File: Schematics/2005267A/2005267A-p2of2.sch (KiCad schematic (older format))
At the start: 4 parts, among them J3 ConnectorA1-300, J4 ConnectorA1-400, X2 ArrowTwiddle, X3 ArrowTwiddle

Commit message: Finished sheet 2 (and hence the complete set of sheets) of CAD drawing 2005267A.
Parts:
- removed X2, X3: ArrowTwiddle, symbol AGC_DSKY:ArrowTwiddle
- added G301: Ground-chassis, symbol AGC_DSKY:Ground-chassis
- added unit 22 of J3
- added unit 59 of J3
- added unit 57 of J3
- added unit 54 of J3
- added unit 55 of J3
- added unit 58 of J3
- added unit 50 of J3
- added unit 53 of J3
- added unit 52 of J3
- added unit 26 of J3
- added unit 41 of J3
- added unit 46 of J3
- added unit 44 of J3
- added unit 45 of J3
- added unit 71 of J3
- added unit 70 of J3
- added unit 62 of J3
- added unit 68 of J3
- added unit 69 of J3
- added unit 61 of J3
- added unit 63 of J3
- added unit 64 of J3
- added unit 65 of J3
- added unit 66 of J3
- added unit 67 of J3
- added unit 1 of J3
- added unit 19 of J3
- added unit 18 of J3
- added unit 42 of J3
- added unit 11 of J3
- added unit 10 of J3
- added unit 15 of J3
- added unit 43 of J3
- added unit 8 of J3
- added unit 9 of J3
- added unit 6 of J3
- added unit 4 of J3
- added unit 38 of J3
- added unit 56 of J3
- added unit 3 of J3
- added unit 37 of J3
- added unit 35 of J3
- added unit 34 of J3
- added unit 33 of J3
- added unit 32 of J3
- added unit 31 of J3
- added unit 30 of J3
- added unit 39 of J3
- added unit 17 of J3
- added unit 7 of J3
- added unit 5 of J3
- added unit 2 of J3
- added unit 40 of J3
- added unit 16 of J3
- added unit 13 of J3
- added unit 47 of J3
- added unit 25 of J3
- added unit 14 of J3
- added unit 27 of J3
- added unit 20 of J3
- added unit 23 of J3
- added unit 49 of J3
- added unit 29 of J3
- added unit 28 of J3
- added unit 64 of J4
- added unit 68 of J4
- added unit 61 of J4
- added unit 62 of J4
- added unit 63 of J4
- added unit 4 of J4
- added unit 28 of J4
- added unit 71 of J4
- added unit 1 of J4
- added unit 3 of J4
- added unit 2 of J4
- added unit 5 of J4
- added unit 7 of J4
- added unit 6 of J4
- added unit 9 of J4
- added unit 8 of J4
- added unit 22 of J4
- added unit 67 of J4
- added unit 65 of J4
- added unit 16 of J4
- added unit 17 of J4
- added unit 14 of J4
- added unit 15 of J4
- added unit 13 of J4
- added unit 10 of J4
- added unit 11 of J4
- added unit 18 of J4
- added unit 19 of J4
- added unit 32 of J4
- added unit 31 of J4
- added unit 30 of J4
- added unit 37 of J4
- added unit 29 of J4
- added unit 25 of J4
- added unit 66 of J4
- added unit 69 of J4
- added unit 38 of J4
- added unit 39 of J4
- added unit 35 of J4
- added unit 49 of J4
- added unit 45 of J4
- added unit 44 of J4
- added unit 47 of J4
- added unit 34 of J4
- added unit 46 of J4
- added unit 41 of J4
- added unit 40 of J4
- added unit 43 of J4
- added unit 42 of J4
- added unit 70 of J4
- added unit 54 of J4
- added unit 27 of J4
- added unit 26 of J4
- added unit 23 of J4
- added unit 55 of J4
- added unit 57 of J4
- added unit 56 of J4
- added unit 50 of J4
- added unit 53 of J4
- added unit 52 of J4
- added unit 59 of J4
- added unit 58 of J4
- added unit 20 of J4
- added unit 33 of J4
- added U201: D3NOR-+4SW-0VDCA-CB_-E_F, symbol D3NOR-+4SW-0VDCA:D3NOR-+4SW-0VDCA-CB_-E_F
- added U202, U207, U211, U213, U217, U219, U223, U225, U229, U233: D3NOR-+4SW-0VDCA-CB_-EF_, symbol D3NOR-+4SW-0VDCA:D3NOR-+4SW-0VDCA-CB_-EF_
- added U203, U215, U221, U227, U246: D3NOR-FAP-0VDCA-expander-BAC-EDF, symbol D3NOR-FAP-0VDCA-expander:D3NOR-FAP-0VDCA-expander-BAC-EDF
- added U204, U210, U216, U222, U228, U239: D3NOR-+4SW-0VDCA-BC_-EF_, symbol D3NOR-+4SW-0VDCA:D3NOR-+4SW-0VDCA-BC_-EF_
- added U205, U235, U238, U241, U244: D3NOR-+4SW-0VDCA-CB_-FE_, symbol D3NOR-+4SW-0VDCA:D3NOR-+4SW-0VDCA-CB_-FE_
- added U206, U208, U212, U214, U218, U220, U224, U226, U230, U231, U236, U237, U242, U243: D3NOR-+4SW-0VDCA-BC_-E_F, symbol D3NOR-+4SW-0VDCA:D3NOR-+4SW-0VDCA-BC_-E_F
- added U209: D3NOR-FAP-0VDCA-expander-BAC-DEF, symbol D3NOR-FAP-0VDCA-expander:D3NOR-FAP-0VDCA-expander-BAC-DEF
- added U232: D3NOR-+4SW-0VDCA-BC_-FE_, symbol D3NOR-+4SW-0VDCA:D3NOR-+4SW-0VDCA-BC_-FE_
- added U234, U240: D3NOR-FAP-0VDCA-expander-ABC-DFE, symbol D3NOR-FAP-0VDCA-expander:D3NOR-FAP-0VDCA-expander-ABC-DFE
- added U245: D3NOR-+4SW-0VDCA-CB_-DFE, symbol D3NOR-+4SW-0VDCA:D3NOR-+4SW-0VDCA-CB_-DFE
- added U247, U253, U256, U258: D3NOR-+4SW-0VDCA-_C_-_F_, symbol D3NOR-+4SW-0VDCA:D3NOR-+4SW-0VDCA-_C_-_F_
- added U248, U259: D3NOR-+4SW-0VDCA-_C_-DEF, symbol D3NOR-+4SW-0VDCA:D3NOR-+4SW-0VDCA-_C_-DEF
- added U249: D3NOR-+4SW-0VDCA-_C_-FE_, symbol D3NOR-+4SW-0VDCA:D3NOR-+4SW-0VDCA-_C_-FE_
- added U250: D3NOR-+4SW-0VDCA-_C_-F__, symbol D3NOR-+4SW-0VDCA:D3NOR-+4SW-0VDCA-_C_-F__
- added U251: D3NOR-+4SW-0VDCA-C__-FE_, symbol D3NOR-+4SW-0VDCA:D3NOR-+4SW-0VDCA-C__-FE_
- added U252: D3NOR-+4SW-0VDCA-_C_-EDF, symbol D3NOR-+4SW-0VDCA:D3NOR-+4SW-0VDCA-_C_-EDF
- added U254: D3NOR-+4SW-0VDCA-_C_-DFE, symbol D3NOR-+4SW-0VDCA:D3NOR-+4SW-0VDCA-_C_-DFE
- added U255: D3NOR-+4SW-0VDCA-_C_-EF_, symbol D3NOR-+4SW-0VDCA:D3NOR-+4SW-0VDCA-_C_-EF_
- added U257: D3NOR-+4SW-0VDCA-C__-EF_, symbol D3NOR-+4SW-0VDCA:D3NOR-+4SW-0VDCA-C__-EF_
- added U260: D3NOR-+4SW-0VDCA-ACB-DEF, symbol D3NOR-+4SW-0VDCA:D3NOR-+4SW-0VDCA-ACB-DEF
- added X301, X302, X303, X304, X305: ArrowTwiddle, symbol AGC_DSKY:ArrowTwiddle
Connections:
- net +4SW: now also U201.10 (+4SW), U202.10 (+4SW), U204.10 (+4SW), U205.10 (+4SW), U206.10 (+4SW), U207.10 (+4SW), U208.10 (+4SW), U210.10 (+4SW), U211.10 (+4SW), U212.10 (+4SW), U213.10 (+4SW), U214.10 (+4SW), U216.10 (+4SW), U217.10 (+4SW), U218.10 (+4SW), U219.10 (+4SW), U220.10 (+4SW), U222.10 (+4SW), U223.10 (+4SW), U224.10 (+4SW), U225.10 (+4SW), U226.10 (+4SW), U228.10 (+4SW), U229.10 (+4SW), U230.10 (+4SW), U231.10 (+4SW), U232.10 (+4SW), U233.10 (+4SW), U235.10 (+4SW), U236.10 (+4SW), U237.10 (+4SW), U238.10 (+4SW), U239.10 (+4SW), U241.10 (+4SW), U242.10 (+4SW), U243.10 (+4SW), U244.10 (+4SW), U245.10 (+4SW), U247.10 (+4SW), U248.10 (+4SW), U249.10 (+4SW), U250.10 (+4SW), U251.10 (+4SW), U252.10 (+4SW), U253.10 (+4SW), U254.10 (+4SW), U255.10 (+4SW), U256.10 (+4SW), U257.10 (+4SW), U258.10 (+4SW), U259.10 (+4SW), U260.10 (+4SW), X303.1 (pwr), X305.1 (pwr)
- net 0VDCA: now also U201.4 (0VDCA), U201.5 (0VDCA), U201.6 (0VDCA), U202.4 (0VDCA), U202.5 (0VDCA), U202.6 (0VDCA), U203.5 (0VDCA), U204.4 (0VDCA), U204.5 (0VDCA), U204.6 (0VDCA), U205.4 (0VDCA), U205.5 (0VDCA), U205.6 (0VDCA), U206.4 (0VDCA), U206.5 (0VDCA), U206.6 (0VDCA), U207.4 (0VDCA), U207.5 (0VDCA), U207.6 (0VDCA), U208.4 (0VDCA), U208.5 (0VDCA), U208.6 (0VDCA), U209.5 (0VDCA), U210.4 (0VDCA), U210.5 (0VDCA), U210.6 (0VDCA), U211.4 (0VDCA), U211.5 (0VDCA), U211.6 (0VDCA), U212.4 (0VDCA), U212.5 (0VDCA), U212.6 (0VDCA), U213.4 (0VDCA), U213.5 (0VDCA), U213.6 (0VDCA), U214.4 (0VDCA), U214.5 (0VDCA), U214.6 (0VDCA), U215.5 (0VDCA), U216.4 (0VDCA), U216.5 (0VDCA), U216.6 (0VDCA), U217.4 (0VDCA), U217.5 (0VDCA), U217.6 (0VDCA), U218.4 (0VDCA), U218.5 (0VDCA), U218.6 (0VDCA), U219.4 (0VDCA), U219.5 (0VDCA), U219.6 (0VDCA), U220.4 (0VDCA), U220.5 (0VDCA), U220.6 (0VDCA), U221.5 (0VDCA), U222.4 (0VDCA), U222.5 (0VDCA), U222.6 (0VDCA), U223.4 (0VDCA), U223.5 (0VDCA), U223.6 (0VDCA), U224.4 (0VDCA), U224.5 (0VDCA), U224.6 (0VDCA), U225.4 (0VDCA), U225.5 (0VDCA), U225.6 (0VDCA), U226.4 (0VDCA), U226.5 (0VDCA), U226.6 (0VDCA), U227.5 (0VDCA), U228.4 (0VDCA), U228.5 (0VDCA), U228.6 (0VDCA), U229.4 (0VDCA), U229.5 (0VDCA), U229.6 (0VDCA), U230.4 (0VDCA), U230.5 (0VDCA), U230.6 (0VDCA), U231.4 (0VDCA), U231.5 (0VDCA), U231.6 (0VDCA), U232.4 (0VDCA), U232.5 (0VDCA), U232.6 (0VDCA), U233.4 (0VDCA), U233.5 (0VDCA), U233.6 (0VDCA), U234.5 (0VDCA), U235.4 (0VDCA), U235.5 (0VDCA), U235.6 (0VDCA), U236.4 (0VDCA), U236.5 (0VDCA), U236.6 (0VDCA), U237.4 (0VDCA), U237.5 (0VDCA), U237.6 (0VDCA), U238.4 (0VDCA), U238.5 (0VDCA), U238.6 (0VDCA), U239.4 (0VDCA), U239.5 (0VDCA), U239.6 (0VDCA), U240.5 (0VDCA), U241.4 (0VDCA), U241.5 (0VDCA), U241.6 (0VDCA), U242.4 (0VDCA), U242.5 (0VDCA), U242.6 (0VDCA), U243.4 (0VDCA), U243.5 (0VDCA), U243.6 (0VDCA), U244.4 (0VDCA), U244.5 (0VDCA), U244.6 (0VDCA), U245.4 (0VDCA), U245.5 (0VDCA), U246.5 (0VDCA), U247.3 (0VDCA), U247.4 (0VDCA), U247.5 (0VDCA), U247.6 (0VDCA), U247.7 (0VDCA), U248.3 (0VDCA), U248.4 (0VDCA), U248.5 (0VDCA), U249.3 (0VDCA), U249.4 (0VDCA), U249.5 (0VDCA), U249.6 (0VDCA), U250.3 (0VDCA), U250.4 (0VDCA), U250.5 (0VDCA), U250.6 (0VDCA), U250.7 (0VDCA), U251.3 (0VDCA), U251.4 (0VDCA), U251.5 (0VDCA), U251.6 (0VDCA), U252.3 (0VDCA), U252.4 (0VDCA), U252.5 (0VDCA), U253.3 (0VDCA), U253.4 (0VDCA), U253.5 (0VDCA), U253.6 (0VDCA), U253.7 (0VDCA), U254.3 (0VDCA), U254.4 (0VDCA), U254.5 (0VDCA), U255.3 (0VDCA), U255.4 (0VDCA), U255.5 (0VDCA), U255.6 (0VDCA), U256.3 (0VDCA), U256.4 (0VDCA), U256.5 (0VDCA), U256.6 (0VDCA), U256.7 (0VDCA), U257.3 (0VDCA), U257.4 (0VDCA), U257.5 (0VDCA), U257.6 (0VDCA), U258.3 (0VDCA), U258.4 (0VDCA), U258.5 (0VDCA), U258.6 (0VDCA), U258.7 (0VDCA), U259.3 (0VDCA), U259.4 (0VDCA), U259.5 (0VDCA), U260.5 (0VDCA), X302.1 (pwr), X304.1 (pwr)
- new net: J3.322, U209.3 (B)
- new net: G301.1, J4.401
- new net: J3.359, U224.1 (J)
- new net: J3.357, U224.8 (F)
- new net: J3.354, U221.2 (C)
- new net: J3.355, U222.9 (K)
- new net: J4.464, U260.4 (A)
- new net: J3.346, U221.1 (J)
- new net: J3.350, U221.3 (B)
- new net: U220.1 (J), U221.4 (A)
- new net: U221.6 (D), U222.1 (J)
- new net: J3.352, U221.7 (E)
- new net: J3.353, U221.8 (F)
- new net: J3.344, U221.9 (K)
- new net: J3.358, U227.9 (K)
- new net: J4.468, U260.9 (K)
- new net: J4.461, U259.7 (E)
- new net: J4.462, U259.8 (F)
- new net: J4.463, U258.1 (J), U258.9 (K), U259.1 (J)
- new net: U208.1 (J), U209.7 (E)
- new net: U207.2 (C), U207.9 (K), U208.2 (C), U210.7 (E), U210.8 (F)
- new net: J4.442, U202.2 (C), U204.3 (B), U208.3 (B), U210.3 (B), U214.3 (B), U216.3 (B), U220.3 (B), U222.3 (B), U226.3 (B), U228.3 (B), U233.2 (C), U236.3 (B), U239.3 (B), U242.3 (B), U245.2 (C), U251.1 (J), U252.1 (J), U253.1 (J)
- new net: J4.430, U201.7 (E), U206.7 (E), U208.7 (E), U212.7 (E), U214.7 (E), U218.7 (E), U220.7 (E), U224.7 (E), U226.7 (E), U230.7 (E), U231.7 (E), U236.7 (E), U237.7 (E), U242.7 (E), U243.7 (E), U247.1 (J), U247.9 (K), U248.1 (J)
- new net: J3.318, U208.8 (F)
- new net: U207.8 (F), U208.9 (K)
- new net: U205.1 (J), U205.8 (F)
- new net: U204.2 (C), U205.2 (C), U205.9 (K), U206.2 (C), U206.3 (B)
- new net: J4.406, U201.3 (B), U205.3 (B), U207.3 (B), U211.3 (B), U213.3 (B), U217.3 (B), U219.3 (B), U223.3 (B), U225.3 (B), U229.3 (B), U232.2 (C), U235.3 (B), U238.3 (B), U241.3 (B), U244.3 (B), U249.1 (J), U250.1 (J), U250.9 (K)
- new net: U205.7 (E), U206.9 (K)
- new net: J4.404, U234.6 (D)
- new net: J3.326, U210.9 (K)
- new net: J4.418, U240.6 (D)
- new net: J4.422, U240.7 (E)
- new net: U240.8 (F), U242.1 (J)
- new net: J4.426, U240.9 (K)
- new net: J4.425, U240.1 (J)
- new net: J4.427, U240.2 (C)
- new net: U239.1 (J), U240.3 (B)
- new net: J4.420, U240.4 (A)
- new net: J4.434, U246.6 (D)
- new net: J4.437, U246.7 (E)
- new net: J4.440, U246.8 (F)
- new net: J4.438, U246.9 (K)
- new net: J4.439, U246.1 (J)
- new net: J4.441, U246.2 (C)
- new net: J4.433, U246.3 (B)
- new net: U245.1 (J), U246.4 (A)
- new net: J4.417, U237.8 (F)
- new net: U237.9 (K), U238.7 (E)
- new net: J4.416, U237.1 (J)
- new net: U237.2 (C), U237.3 (B), U238.2 (C), U238.9 (K), U239.2 (C)
- new net: J4.414, U236.8 (F)
- new net: U235.7 (E), U236.9 (K)
- new net: U234.8 (F), U236.1 (J)
- new net: U233.7 (E), U233.8 (F), U235.2 (C), U235.9 (K), U236.2 (C)
- new net: U235.1 (J), U235.8 (F)
- new net: U209.4 (A), U210.1 (J)
- new net: U210.2 (C), U211.2 (C), U211.9 (K), U212.2 (C), U212.3 (B)
- new net: J3.343, U218.8 (F)
- new net: U217.8 (F), U218.9 (K)
- new net: J3.345, U218.1 (J)
- new net: U216.2 (C), U217.2 (C), U217.9 (K), U218.2 (C), U218.3 (B)
- new net: J3.333, U214.8 (F)
- new net: U213.8 (F), U214.9 (K)
- new net: U214.1 (J), U215.4 (A)
- new net: U213.2 (C), U213.9 (K), U214.2 (C), U216.7 (E), U216.8 (F)
- new net: U217.1 (J), U217.7 (E)
- new net: J3.340, U216.9 (K)
- new net: U215.6 (D), U216.1 (J)
- new net: U211.1 (J), U211.7 (E)
- new net: U211.8 (F), U212.9 (K)
- new net: J4.405, U233.9 (K)
- new net: U213.1 (J), U213.7 (E)
- new net: J3.328, U212.8 (F)
- new net: J3.331, U212.1 (J)
- new net: U201.1 (J), U202.7 (E)
- new net: U201.9 (K), U202.8 (F)
- new net: U201.2 (C), U202.3 (B), U202.9 (K), U204.7 (E), U204.8 (F)
- new net: U202.1 (J), U203.6 (D)
- new net: J3.304, U201.8 (F)
- new net: J3.314, U206.8 (F)
- new net: J3.316, U206.1 (J)
- new net: U207.1 (J), U207.7 (E)
- new net: J3.311, U204.9 (K)
- new net: U203.4 (A), U204.1 (J)
- new net: J3.347, U220.8 (F)
- new net: U219.8 (F), U220.9 (K)
- new net: U228.2 (C), U229.2 (C), U229.7 (E), U229.8 (F), U230.1 (J)
- new net: J3.369, U229.9 (K)
- new net: U227.6 (D), U228.1 (J)
- new net: U225.2 (C), U225.9 (K), U226.2 (C), U228.7 (E), U228.8 (F)
- new net: J3.368, U228.9 (K)
- new net: U223.1 (J), U223.7 (E)
- new net: U222.2 (C), U223.2 (C), U223.9 (K), U224.2 (C), U224.3 (B)
- new net: U223.8 (F), U224.9 (K)
- new net: U219.2 (C), U219.9 (K), U220.2 (C), U222.7 (E), U222.8 (F)
- new net: U229.1 (J), U230.3 (B)
- new net: U226.1 (J), U227.4 (A)
- new net: J3.362, U226.8 (F)
- new net: U225.8 (F), U226.9 (K)
- new net: U225.1 (J), U225.7 (E)
- new net: J4.409, U234.1 (J)
- new net: J4.413, U234.2 (C)
- new net: U233.1 (J), U234.3 (B)
- new net: J4.408, U234.4 (A)
- new net: J4.407, U234.7 (E)
- new net: J4.411, U234.9 (K)
- new net: J4.471, U260.6 (D)
- new net: J3.371, U230.8 (F)
- new net: J3.370, U227.2 (C)
- new net: J4.403, U231.1 (J)
- new net: J4.402, U231.8 (F)
- new net: J3.366, U227.7 (E)
- new net: J3.367, U227.8 (F)
- new net: J3.361, U227.1 (J)
- new net: J3.364, U227.3 (B)
- new net: J4.467, U260.1 (J)
- new net: U231.2 (C), U231.3 (B), U232.3 (B), U232.9 (K), U233.3 (B)
- new net: U231.9 (K), U232.7 (E)
- new net: U232.1 (J), U232.8 (F)
- new net: U230.2 (C), U230.9 (K)
- new net: U239.7 (E), U239.8 (F), U241.2 (C), U241.9 (K), U242.2 (C)
- new net: J4.419, U239.9 (K)
- new net: U238.1 (J), U238.8 (F)
- new net: J4.465, U260.3 (B)
- new net: U244.1 (J), U244.8 (F)
- new net: U243.2 (C), U243.3 (B), U244.2 (C), U244.9 (K), U245.3 (B)
- new net: U241.1 (J), U241.8 (F)
- new net: U241.7 (E), U242.9 (K)
- new net: J4.432, U243.1 (J)
- new net: J4.431, U243.8 (F)
- new net: U243.9 (K), U244.7 (E)
- new net: J4.429, U242.8 (F)
- new net: J4.435, U245.6 (D), U248.7 (E), U251.7 (E)
- new net: J4.450, U245.7 (E), U252.7 (E)
- new net: J4.449, U245.8 (F), U248.6 (D), U251.8 (F), U252.6 (D), U254.7 (E), U257.7 (E)
- new net: U245.9 (K), U247.2 (C), U247.8 (F), U248.2 (C)
- new net: J4.443, U248.8 (F), U254.6 (D)
- new net: U248.9 (K), U249.7 (E)
- new net: J3.301, U203.1 (J)
- new net: J4.446, U249.8 (F), U255.7 (E)
- new net: U249.2 (C), U249.9 (K), U250.2 (C), U250.8 (F)
- new net: J3.306, U203.7 (E)
- new net: J3.310, U203.8 (F)
- new net: J3.303, U203.9 (K)
- new net: J3.309, U203.2 (C)
- new net: J3.308, U203.3 (B)
- new net: J3.315, U209.1 (J)
- new net: J3.320, U209.6 (D)
- new net: J3.325, U209.8 (F)
- new net: J3.317, U209.9 (K)
- new net: U255.9 (K), U256.2 (C), U256.8 (F), U257.2 (C)
- new net: J4.457, U256.1 (J), U256.9 (K), U257.1 (J)
- new net: J4.466, U260.2 (C)
- new net: U251.2 (C), U251.9 (K), U252.2 (C), U253.2 (C)
- new net: U252.9 (K), U253.8 (F), U254.2 (C), U255.2 (C)
- new net: J4.454, U253.9 (K), U254.1 (J), U255.1 (J)
- new net: J4.453, U252.8 (F), U254.8 (F), U257.8 (F)
- new net: U254.9 (K), U255.8 (F)
- new net: U257.9 (K), U258.2 (C), U258.8 (F), U259.2 (C)
- new net: J4.455, U259.6 (D)
- new net: J4.470, U259.9 (K)
- new net: J4.469, U260.7 (E)
- new net: J3.337, U215.7 (E)
- new net: J3.338, U215.8 (F)
- new net: J3.330, U215.9 (K)
- new net: J3.332, U215.1 (J)
- new net: J3.339, U215.2 (C)
- new net: J3.335, U215.3 (B)
- new net: J4.459, U260.8 (F)
- new net: J3.323, U209.2 (C)
- new net: U219.1 (J), U219.7 (E)
- new net FAP: J3.334, U203.10 (FAP), U209.10 (FAP), U215.10 (FAP), U221.10 (FAP), U227.10 (FAP), U234.10 (FAP), U240.10 (FAP), U246.10 (FAP), X301.1 (pwr)
- no-connect marks 0 -> 23
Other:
- note added: "44342\n44348\n44336\n44330\n44324\n44318\n44312\n44306"
- note added: "44406\n44412\n44418\n44424\n44430\n44461\n44354\n44360"
- note added: "CCH10"
- note added: "Notes from the Virtual AGC Project:\n1. This CAD drawing was manually transcribed from the \n original Apollo Program drawing 2005267A, but is not\n itself original to the Apollo Program. — RSB 2018\n2. The original drawing did not show reference \n designators for the components, so this CAD drawing \n does not show them either. For purposes of netlist \n generation and ERC, the NOR gates have r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"
- note added: "RCH10/"
- note added: "SPARE PINS"
- note added: "TO PIN G & UNUSED\nINPUTS OF 44300 &\n44400 SERIES GATES"
- note added: "TO PIN V OF 44300 & 44400\nSERIES GATES EXCEPT\nTHOSE GATES TIED \nTO FAP PIN (334)"
- note added: "TO PIN V OF GATES"
- note added: "WCH10/"
- note removed: "Notes from the Virtual AGC Project:\n1. This CAD drawing was manually transcribed from the original Apollo Program\n drawing 2005267A, but is not itself original to the Apollo Program. — RSB 2018\n2. The original drawing did not show reference designators for the components, so\n this CAD drawing does not show them either. For purposes of netlist generation\n and ERC, the NOR gates have reference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"
- note removed: "TO PIN G &\nUNUSED INPUTS OF \n35300 AND 35400\nSERIES GATES"
- note removed: "TO PIN V OF\n35300 AND 35400\nSERIES GATES \nEXCEPT THOSE \nGATES TIED TO \nFAP PIN (430)"

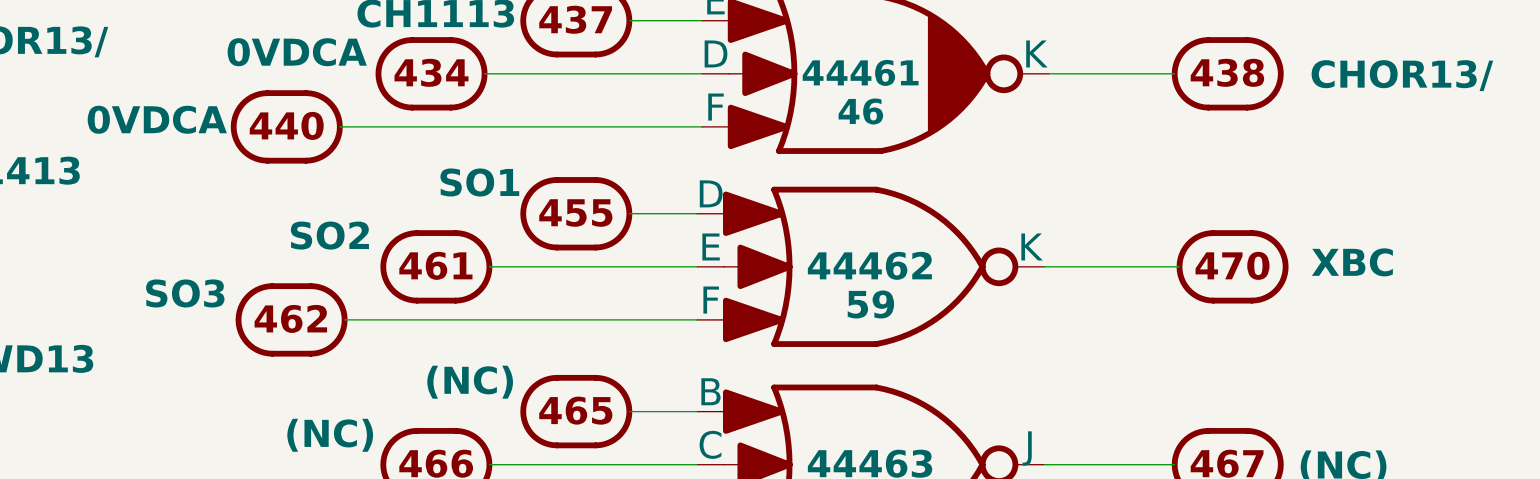
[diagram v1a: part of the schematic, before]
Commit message: Cross-checked/corrected module A17 connector-pad labeling vs pin database.
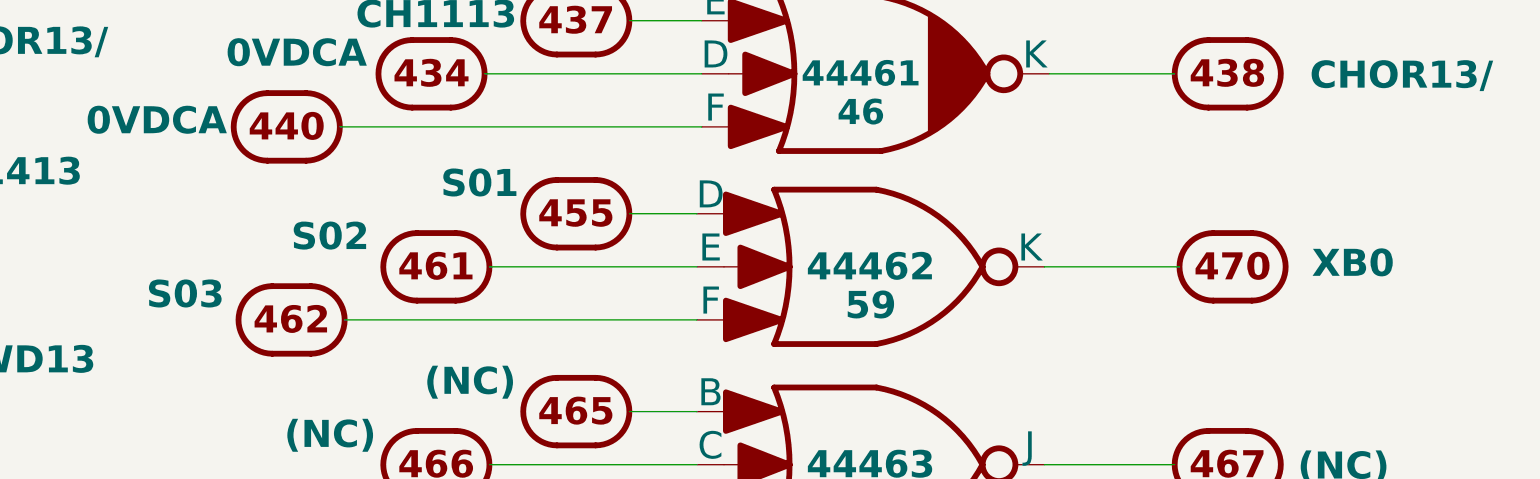
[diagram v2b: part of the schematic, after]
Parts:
- J3, J4: Caption (none) -> 0VDCA
- J3, J4: Caption (none) -> +4SW
- J4: Caption SO2 -> S02
- J4: Caption SO3 -> S03
- J4: Caption XBC -> XB0
- J4: Caption SO1 -> S01
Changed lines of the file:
@@
 F 2 "" H 32675 27375 140 0001 C CNN
 F 3 "" H 32675 27375 140 0001 C CNN
-F 4 "" H 32675 27125 140 0000 C BNB "Caption"
+F 4 "0VDCA" H 32675 27125 140 0001 C BNB "Caption"
 	12   32675 26900
 	1    0    0    -1
@@
 F 2 "" H 26825 28350 140 0001 C CNN
 F 3 "" H 26825 28350 140 0001 C CNN
-F 4 "" H 26825 28100 140 0000 C BNB "Caption"
+F 4 "0VDCA" H 26825 28100 140 0001 C BNB "Caption"
 	60   26825 27875
 	1    0    0    -1
@@
 F 2 "" H 32650 28375 140 0001 C CNN
 F 3 "" H 32650 28375 140 0001 C CNN
-F 4 "" H 32650 28125 140 0000 C BNB "Caption"
+F 4 "0VDCA" H 32650 28125 140 0001 C BNB "Caption"
 	60   32650 27900
 	1    0    0    -1
@@
 F 2 "" H 37150 9300 140 0001 C CNN
 F 3 "" H 37150 9300 140 0001 C CNN
-F 4 "SO2" H 36600 8900 140 0000 C BNB "Caption"
+F 4 "S02" H 36600 8900 140 0000 C BNB "Caption"
 	61   37150 8825
 	1    0    0    -1
@@
 F 2 "" H 36400 9575 140 0001 C CNN
 F 3 "" H 36400 9575 140 0001 C CNN
-F 4 "SO3" H 35850 9150 140 0000 C BNB "Caption"
+F 4 "S03" H 35850 9150 140 0000 C BNB "Caption"
 	62   36400 9100
 	1    0    0    -1
@@
 F 2 "" H 41275 9300 140 0001 C CNN
 F 3 "" H 41275 9300 140 0001 C CNN
-F 4 "XBC" H 40650 8725 140 0000 C BNB "Caption"
+F 4 "XB0" H 40650 8725 140 0000 C BNB "Caption"
 	70   41275 8825
 	-1   0    0    1
@@
 F 2 "" H 32675 27875 140 0001 C CNN
 F 3 "" H 32675 27875 140 0001 C CNN
-F 4 "" H 32675 27625 140 0000 C BNB "Caption"
+F 4 "0VDCA" H 32675 27625 140 0001 C BNB "Caption"
 	36   32675 27400
 	1    0    0    -1
@@
 F 2 "" H 32650 29725 140 0001 C CNN
 F 3 "" H 32650 29725 140 0001 C CNN
-F 4 "" H 32650 29475 140 0000 C BNB "Caption"
+F 4 "+4SW" H 32650 29475 140 0001 C BNB "Caption"
 	48   32650 29250
 	1    0    0    -1
@@
 F 2 "" H 37875 9025 140 0001 C CNN
 F 3 "" H 37875 9025 140 0001 C CNN
-F 4 "SO1" H 37375 8625 140 0000 C BNB "Caption"
+F 4 "S01" H 37375 8625 140 0000 C BNB "Caption"
 	55   37875 8550
 	1    0    0    -1
@@
 F 2 "" H 26850 29225 140 0001 C CNN
 F 3 "" H 26850 29225 140 0001 C CNN
-F 4 "" H 26850 28975 140 0000 C BNB "Caption"
+F 4 "+4SW" H 26850 28975 140 0001 C BNB "Caption"
 	24   26850 28750
 	1    0    0    -1
@@
 F 2 "" H 32675 29250 140 0001 C CNN
 F 3 "" H 32675 29250 140 0001 C CNN
-F 4 "" H 32675 29000 140 0000 C BNB "Caption"
+F 4 "+4SW" H 32675 29000 140 0001 C BNB "Caption"
 	24   32675 28775
 	1    0    0    -1
@@
 F 2 "" H 26825 27350 140 0001 C CNN
 F 3 "" H 26825 27350 140 0001 C CNN
-F 4 "" H 26825 27100 140 0000 C BNB "Caption"
+F 4 "0VDCA" H 26825 27100 140 0001 C BNB "Caption"
 	12   26825 26875
 	1    0    0    -1
